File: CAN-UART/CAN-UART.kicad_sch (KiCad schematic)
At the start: 19 parts, among them CN1 1.0T-4PLTPZ, J1 Conn_01x06, P1 USB_C_Plug_USB2.0, U1 AP2112K-3.3, U2 SN65HVD230, U3 ESP32-C3, U4 AT45DB161D-SU

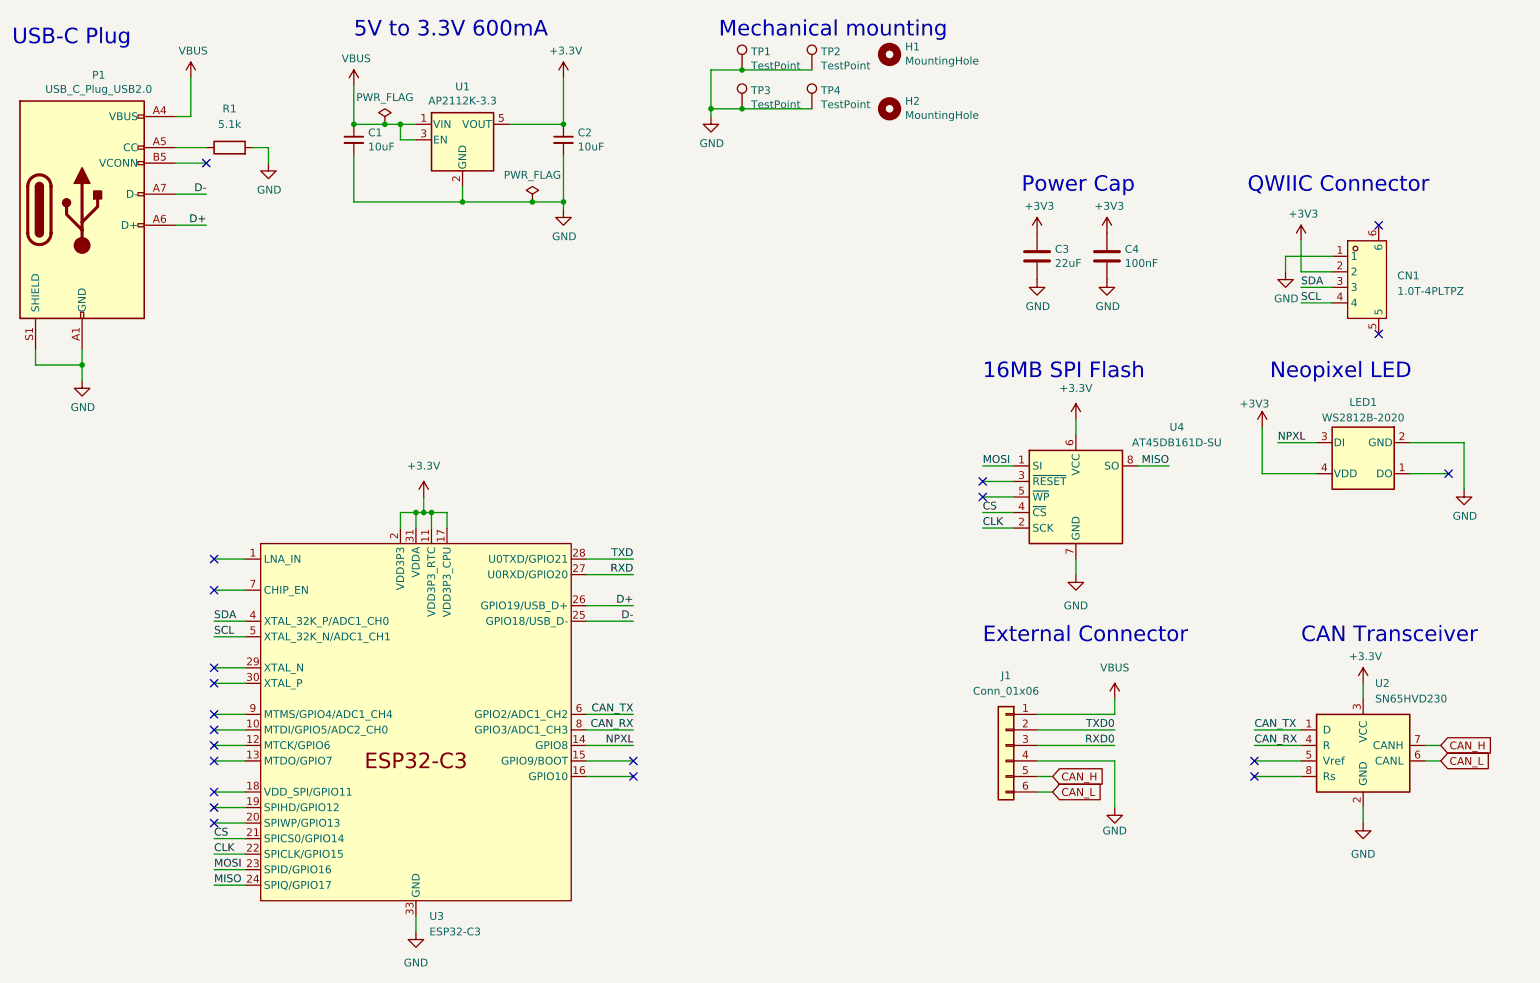
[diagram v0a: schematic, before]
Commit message: Replaced ESP32-C3 with ESP32-C3-MINI-1-U
Removed external Flash
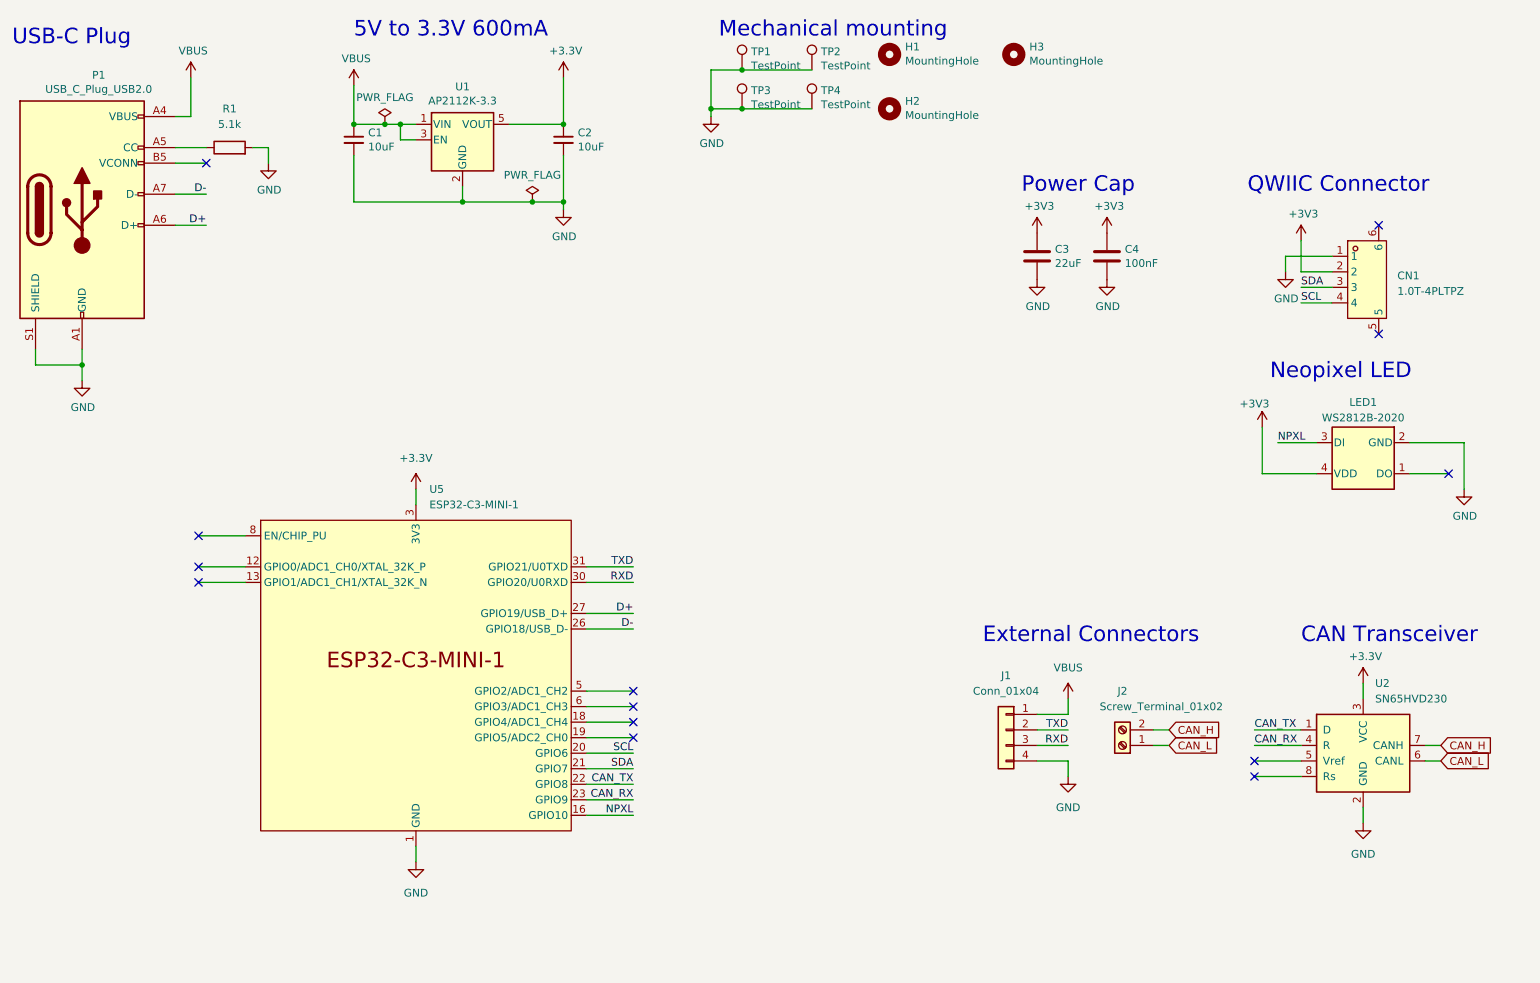
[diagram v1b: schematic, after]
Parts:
- removed J1: Conn_01x06, Connector_PinSocket_2.00mm:PinSocket_1x06_P2.00mm_Horizontal, symbol Connector_Generic:Conn_01x06
- removed U3: ESP32-C3, Package_DFN_QFN:QFN-32-1EP_5x5mm_P0.5mm_EP3.45x3.45mm, symbol Espressif:ESP32-C3
- removed U4: AT45DB161D-SU, Package_SO:SOIC-8_5.275x5.275mm_P1.27mm, symbol Memory_Flash:AT45DB161D-SU
- added H3: MountingHole, MountingHole:MountingHole_2.2mm_M2, symbol Mechanical:MountingHole
- added J1: Conn_01x04, Connector_PinSocket_2.54mm:PinSocket_1x04_P2.54mm_Horizontal, symbol Connector_Generic:Conn_01x04
- added J2: Screw_Terminal_01x02, Connector_PinHeader_2.54mm:PinHeader_1x02_P2.54mm_Horizontal, symbol Connector:Screw_Terminal_01x02
- added U5: ESP32-C3-MINI-1, Espressif:ESP32-C3-MINI-1, symbol Espressif:ESP32-C3-MINI-1
- C3, C4: footprint Capacitor_SMD:C_0402_1005Metric_Pad0.74x0.62mm_HandSolder -> Capacitor_SMD:C_0201_0603Metric_Pad0.64x0.40mm_HandSolder
- R1: footprint (none) -> Resistor_SMD:R_0201_0603Metric_Pad0.64x0.40mm_HandSolder
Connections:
- net +3.3V: now also U5.3 (3V3)
- net CAN_H: now also J2.2 (Pin_2)
- net CAN_L: now also J2.1 (Pin_1)
- net CAN_RX: now also U5.23 (GPIO9)
- net CAN_TX: now also U5.22 (GPIO8)
- net D+: now also U5.27 (GPIO19/USB_D+)
- net D-: now also U5.26 (GPIO18/USB_D-)
- net GND: now also J1.4 (Pin_4), U5.1 (GND), U5.11 (GND), U5.14 (GND), U5.2 (GND), U5.36 (GND), U5.37 (GND), U5.38 (GND), U5.39 (GND), U5.40 (GND), U5.41 (GND), U5.42 (GND), U5.43 (GND), U5.44 (GND), U5.45 (GND), U5.46 (GND), U5.47 (GND), U5.48 (GND), U5.49 (GND), U5.50 (GND), U5.51 (GND), U5.52 (GND), U5.53 (GND)
- net NPXL: now also U5.16 (GPIO10)
- net RXD: now also J1.3 (Pin_3), U5.30 (GPIO20/U0RXD)
- net SCL: now also U5.20 (GPIO6)
- net SDA: now also U5.21 (GPIO7)
- net TXD: now also J1.2 (Pin_2), U5.31 (GPIO21/U0TXD)
- net VBUS: now also J1.1 (Pin_1)
- no-connect marks 21 -> 13
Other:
- note added: "External Connectors"
- note removed: "16MB SPI Flash"
- note removed: "External Connector"

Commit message: Added optional Termination resistor
Two 60R betweeen CAN_L & CAN_H
Two Mosfets to (de)activate the resistor software side
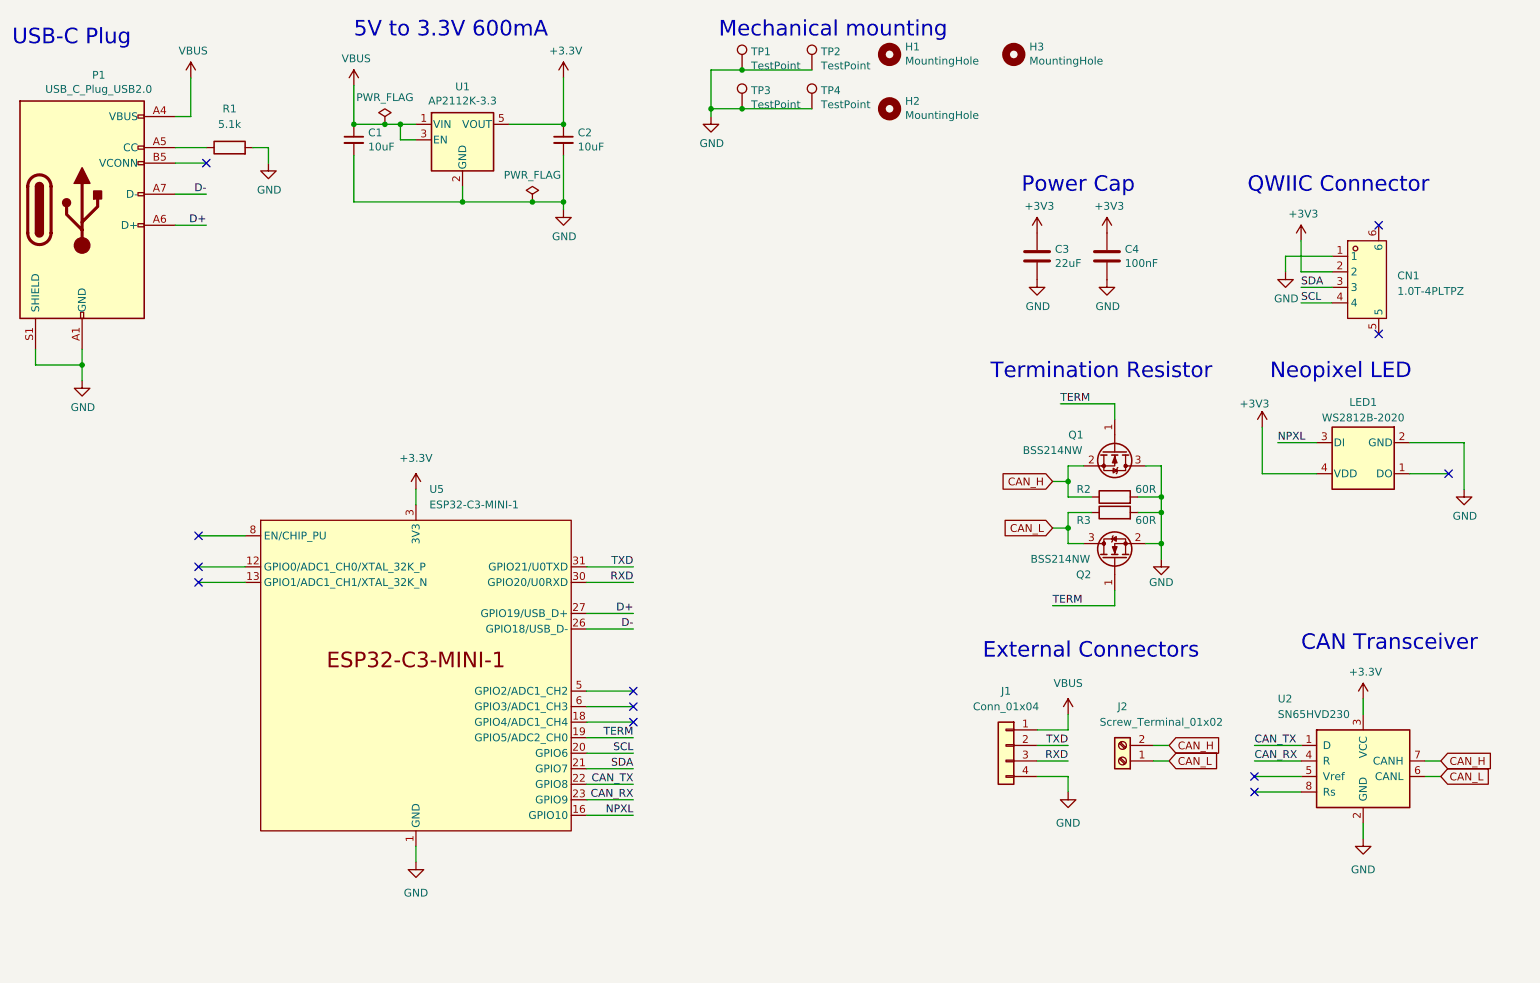
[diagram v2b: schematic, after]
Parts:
- added Q1, Q2: BSS214NW, Package_TO_SOT_SMD:SOT-323_SC-70, symbol Transistor_FET:BSS214NW
- added R2, R3: 60R, symbol Device:R
- P1: footprint Expansion_Card:USB_C_Plug_Molex_105444 -> (none)
- U5: footprint Espressif:ESP32-C3-MINI-1 -> Espressif:ESP32-C3-MINI-1U
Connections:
- net CAN_H: now also Q1.2 (S), R2.1
- net CAN_L: now also Q2.3 (D), R3.1
- net GND: now also Q1.3 (D), Q2.2 (S), R2.2, R3.2
- net TERM: now reaches U5.19 (GPIO5/ADC2_CH0)
- net TERM: now also Q1.1 (G), Q2.1 (G)
- no-connect marks 13 -> 12
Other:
- note added: "Termination Resistor"
- moved on the sheet: J1, J2, U2

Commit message: Updated Schematic
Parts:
- removed H3: MountingHole, MountingHole:MountingHole_2.2mm_M2, symbol Mechanical:MountingHole
- R2, R3: footprint (none) -> Resistor_SMD:R_0402_1005Metric_Pad0.72x0.64mm_HandSolder
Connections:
- net CAN_L: now also Q2.2 (S); no longer Q2.3 (D)
- net GND: now also Q2.3 (D); no longer Q2.2 (S)
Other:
- moved on the sheet: Q2
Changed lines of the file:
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@@
     )
   )
-  (symbol (lib_id "Transistor_FET:BSS214NW") (at 205.74 104.14 90) (unit 1)
-    (in_bom yes) (on_board yes) (dnp no)
-    (property "Reference" "Q2" (at 200.66 106.68 90)
-      (effects (font (size 1.27 1.27)))
-    )
-    (property "Value" "BSS214NW" (at 196.85 104.14 90)
-      (effects (font (size 1.27 1.27)))
-    )
-    (property "Footprint" "Package_TO_SOT_SMD:SOT-323_SC-70" (at 207.645 99.06 0)
+  (symbol (lib_id "Transistor_FET:BSS214NW") (at 205.74 104.14 270) (mirror x) (unit 1)
+    (in_bom yes) (on_board yes) (dnp no)
+    (property "Reference" "Q2" (at 199.39 106.68 90)
+      (effects (font (size 1.27 1.27)))
+    )
+    (property "Value" "BSS214NW" (at 195.58 104.14 90)
+      (effects (font (size 1.27 1.27)))
+    )
+    (property "Footprint" "Package_TO_SOT_SMD:SOT-323_SC-70" (at 203.835 99.06 0)
       (effects (font (size 1.27 1.27) italic) (justify left) hide)
     )
@@
     )
   )
-  (symbol (lib_id "Mechanical:MountingHole") (at 189.23 21.59 0) (unit 1)
-    (in_bom yes) (on_board yes) (dnp no)
-    (property "Reference" "H3" (at 191.77 20.3454 0)
-      (effects (font (size 1.27 1.27)) (justify left))
-    )
-    (property "Value" "MountingHole" (at 191.77 22.6568 0)
-      (effects (font (size 1.27 1.27)) (justify left))
-    )
-    (property "Footprint" "MountingHole:MountingHole_2.2mm_M2" (at 189.23 21.59 0)
-      (effects (font (size 1.27 1.27)) hide)
-    )
-    (property "Datasheet" "~" (at 189.23 21.59 0)
-      (effects (font (size 1.27 1.27)) hide)
-    )
-    (instances
-      (project "CAN-UART"
-        (path "/21020eba-b649-4135-9bee-384d0a5cab58"
-          (reference "H3") (unit 1)
-        )
-      )
-    )
-  )
   (symbol (lib_id "power:+3.3V") (at 91.44 92.71 0) (unit 1)
     (in_bom yes) (on_board yes) (dnp no) (fields_autoplaced)
@@
       (effects (font (size 1.27 1.27)))
     )
-    (property "Footprint" "" (at 205.74 95.758 90)
+    (property "Footprint" "Resistor_SMD:R_0402_1005Metric_Pad0.72x0.64mm_HandSolder" (at 205.74 95.758 90)
       (effects (font (size 1.27 1.27)) hide)
     )
@@
       (effects (font (size 1.27 1.27)))
     )
-    (property "Footprint" "" (at 205.74 98.298 90)
-      (effects (font (size 1.27 1.27)) hide)
-    )
+    (property "Footprint" "Resistor_SMD:R_0402_1005Metric_Pad0.72x0.64mm_HandSolder" (at 205.74 98.298 90)
+      (effects (font (size 1.27 1.27)) hide)
+    )
